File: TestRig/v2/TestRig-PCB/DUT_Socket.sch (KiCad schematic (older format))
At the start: 14 parts, among them J201 DUT_CONN, U201 74LS165, U202 74LS165, U203 74LS165

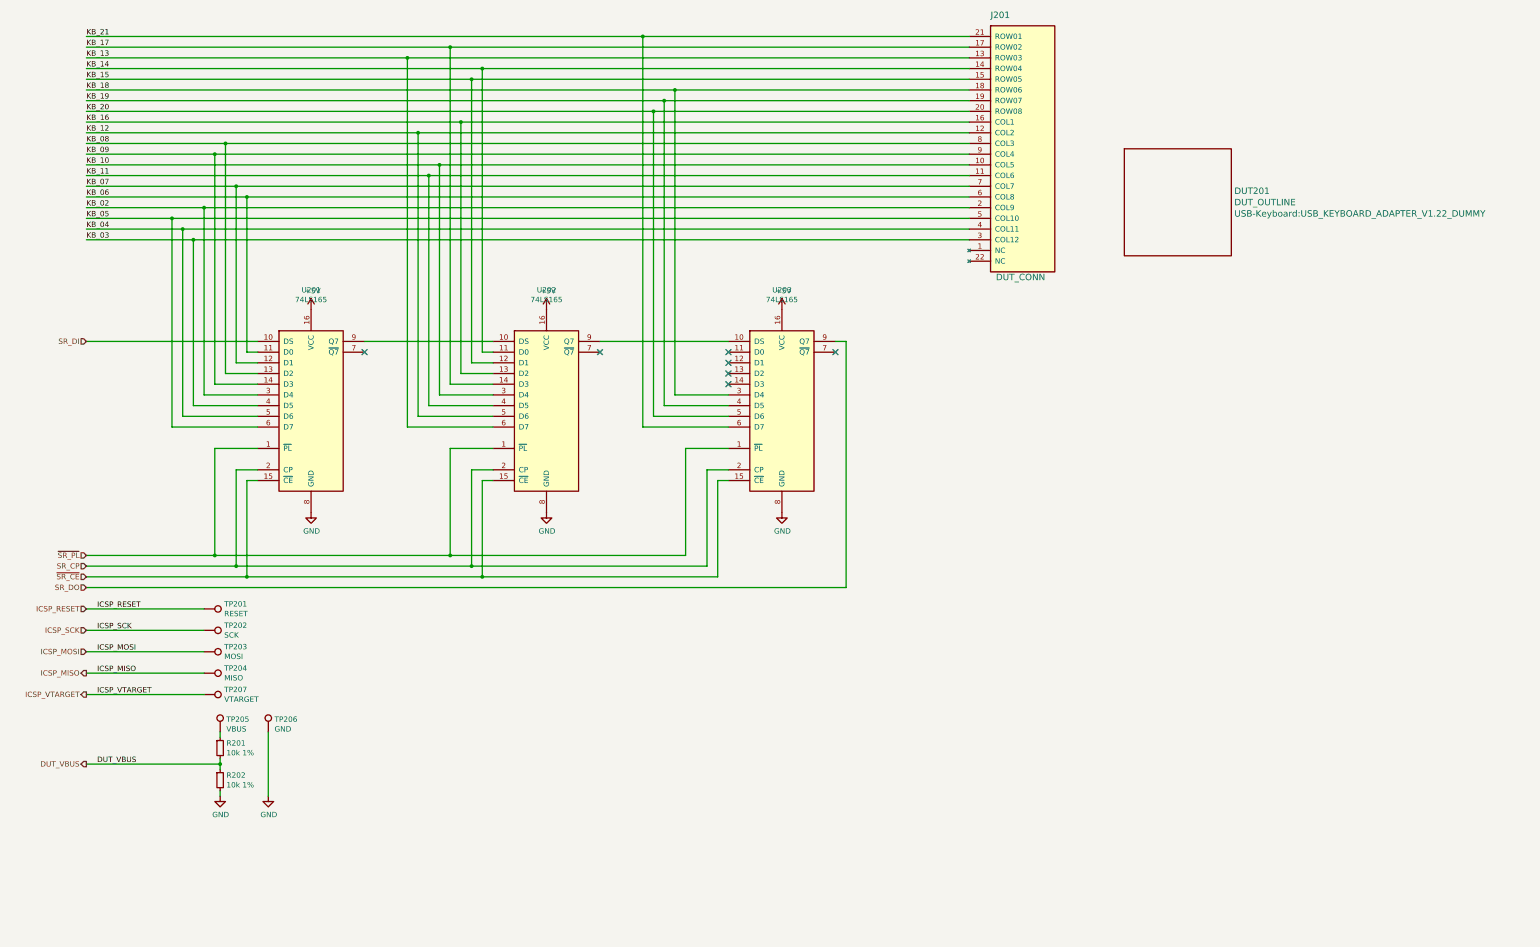
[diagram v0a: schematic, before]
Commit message: Adds working test rig
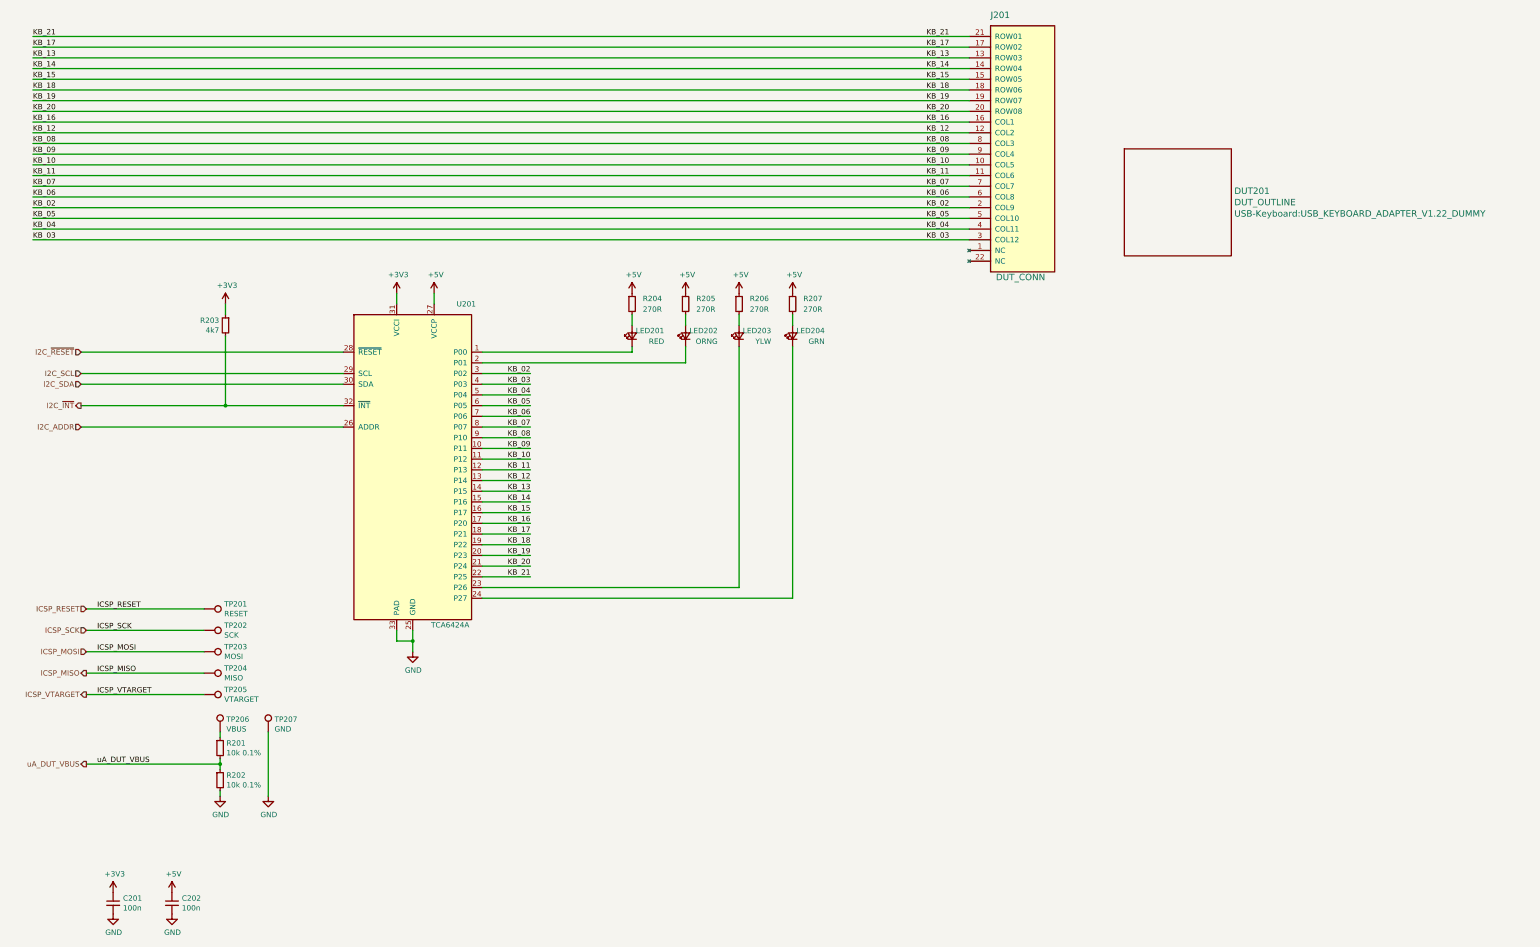
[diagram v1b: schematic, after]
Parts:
- removed U201, U202, U203: 74LS165, Package_SO:TSSOP-16-1EP_4.4x5mm_P0.65mm, symbol 74xx:74LS165
- added C201, C202: 100n, Capacitor_SMD:C_0603_1608Metric, symbol Device:C_Small
- added LED201: RED, LED_SMD:LED_0603_1608Metric, symbol Device:LED_Small
- added LED202: ORNG, LED_SMD:LED_0603_1608Metric, symbol Device:LED_Small
- added LED203: YLW, LED_SMD:LED_0603_1608Metric, symbol Device:LED_Small
- added LED204: GRN, LED_SMD:LED_0603_1608Metric, symbol Device:LED_Small
- added R203: 4k7, Resistor_SMD:R_0603_1608Metric, symbol Device:R_Small
- added R204, R205, R206, R207: 270R, Resistor_SMD:R_0603_1608Metric, symbol Device:R_Small
- added U201: TCA6424A, Package_DFN_QFN:QFN-32-1EP_5x5mm_P0.5mm_EP3.1x3.1mm, symbol rbv_interface:TCA6424A
- J201: MPN (none) -> FH12A-22S-0.5SH(55); Manufacturer (none) -> Hirose
- R201, R202: value 10k 1% -> 10k 0.1%; MPN (none) -> ERA-3AEB103V; Manufacturer (none) -> Panasonic
- renumbered TP207 to TP205, TP205 to TP206, TP206 to TP207
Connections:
- net +5V: now also C202.1, R204.1, R205.1, R206.1, R207.1, U201.27 (VCCP)
- net GND: now also C201.2, C202.2, U201.25 (GND), U201.33 (PAD)
- net KB_02: now also U201.3 (P02)
- net KB_03: now also U201.4 (P03)
- net KB_04: now also U201.5 (P04)
- net KB_05: now also U201.6 (P05)
- net KB_06: now also U201.7 (P06)
- net KB_07: now also U201.8 (P07)
- net KB_08: now also U201.9 (P10)
- net KB_09: now also U201.10 (P11)
- net KB_10: now also U201.11 (P12)
- net KB_11: now also U201.12 (P13)
- net KB_12: now also U201.13 (P14)
- net KB_13: now also U201.14 (P15)
- net KB_14: now also U201.15 (P16)
- net KB_15: now also U201.16 (P17)
- net KB_16: now also U201.17 (P20)
- net KB_17: now also U201.18 (P21)
- net KB_18: now also U201.19 (P22)
- net KB_19: now also U201.20 (P23)
- net KB_20: now also U201.21 (P24)
- net KB_21: now also U201.22 (P25)
- net DUT_VBUS renamed uA_DUT_VBUS
- new net: LED201.1 (K), U201.1 (P00)
- new net: LED202.1 (K), U201.2 (P01)
- new net: LED203.1 (K), U201.23 (P26)
- new net: LED204.1 (K), U201.24 (P27)
- new net: LED201.2 (A), R204.2
- new net: LED202.2 (A), R205.2
- new net: LED203.2 (A), R206.2
- new net: LED204.2 (A), R207.2
- new net +3V3: C201.1, R203.1, U201.31 (VCCI)
- new net I2C_ADDR: U201.26 (ADDR)
- new net I2C_SCL: U201.29 (SCL)
- new net I2C_SDA: U201.30 (SDA)
- new net I2C_~INT: R203.2, U201.32 (~INT)
- new net I2C_~RESET: U201.28 (~RESET)
- no-connect marks 7 -> 0
